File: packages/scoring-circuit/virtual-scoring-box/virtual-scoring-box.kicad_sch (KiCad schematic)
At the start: 0 parts

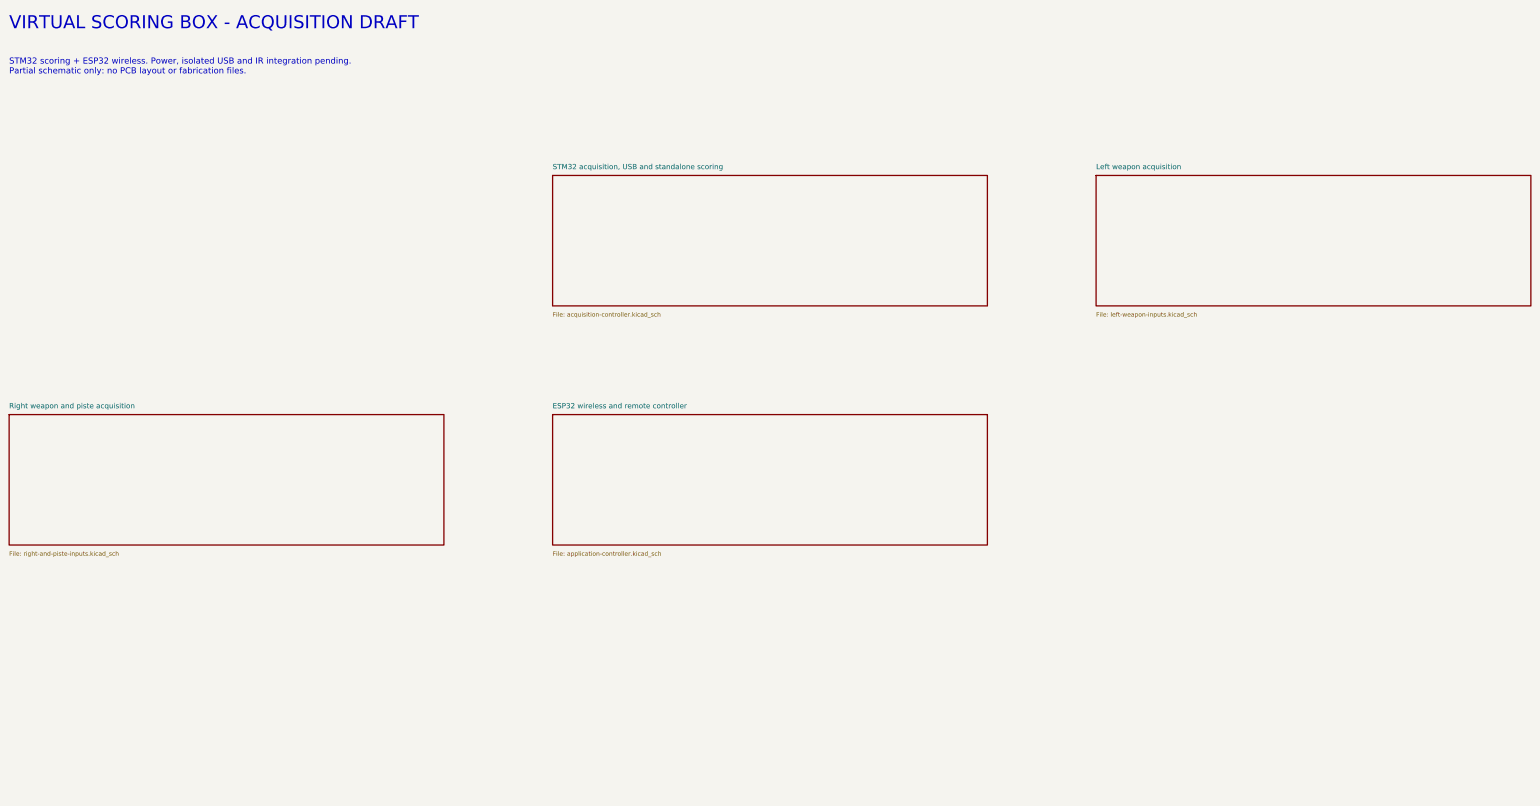
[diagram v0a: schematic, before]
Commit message: feat(scoring-circuit): place virtual scoring box input and controller circuits
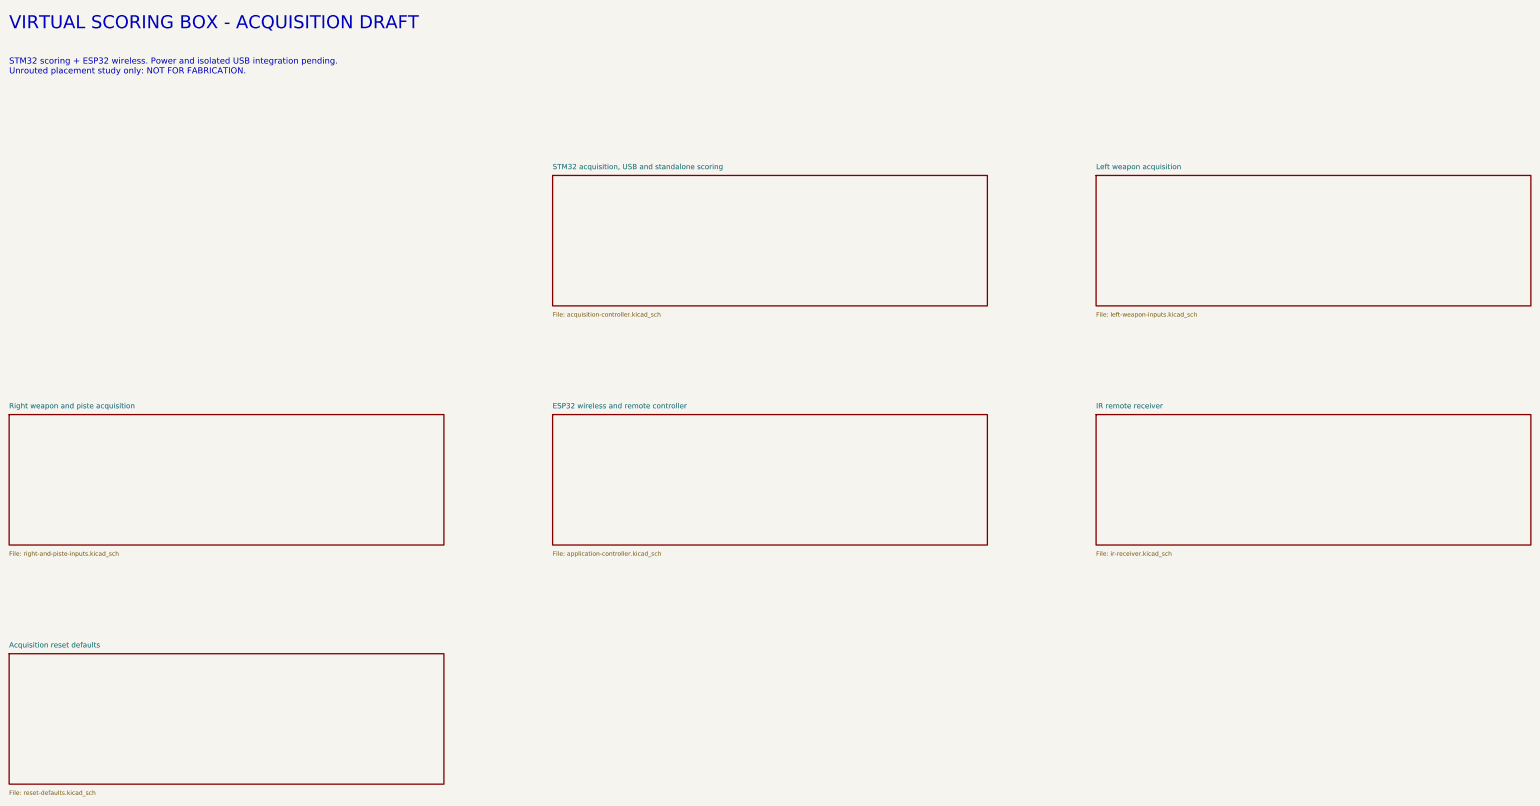
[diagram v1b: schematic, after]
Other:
- added sheet Acquisition reset defaults (reset-defaults.kicad_sch)
- added sheet IR remote receiver (ir-receiver.kicad_sch)
- note added: "STM32 scoring + ESP32 wireless. Power and isolated USB integration pending. Unrouted placement study only: NOT FOR FABRICATION."
- note removed: "STM32 scoring + ESP32 wireless. Power, isolated USB and IR integration pending. Partial schematic only: no PCB layout or fabrication files."
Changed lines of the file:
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@@
 (title_block (title "Virtual scoring box") (rev "Engineering draft") (comment 1 "Separate design - original prototype preserved"))
 (text "VIRTUAL SCORING BOX - ACQUISITION DRAFT" (at 30 20 0) (effects (font (size 3 3)) (justify left)))
-(text "STM32 scoring + ESP32 wireless. Power, isolated USB and IR integration pending.\nPartial schematic only: no PCB layout or fabrication files." (at 30 30 0) (effects (font (size 1.4 1.4)) (justify left)))
+(text "STM32 scoring + ESP32 wireless. Power and isolated USB integration pending.\nUnrouted placement study only: NOT FOR FABRICATION." (at 30 30 0) (effects (font (size 1.4 1.4)) (justify left)))
 (sheet (at 155 55) (size 100 30) (stroke (width 0.2) (type default)) (fill (color 0 0 0 0)) (property "Sheetname" "STM32 acquisition, USB and standalone scoring" (at 155 53 0) (effects (font (size 1.2 1.2)) (justify left))) (property "Sheetfile" "acquisition-controller.kicad_sch" (at 155 87 0) (effects (font (size 1 1)) (justify left))) (instances (project "virtual-scoring-box" (path "/20cc8167-128c-446a-a106-f942323e143f" (page "3")))))
 (sheet (at 280 55) (size 100 30) (stroke (width 0.2) (type default)) (fill (color 0 0 0 0)) (property "Sheetname" "Left weapon acquisition" (at 280 53 0) (effects (font (size 1.2 1.2)) (justify left))) (property "Sheetfile" "left-weapon-inputs.kicad_sch" (at 280 87 0) (effects (font (size 1 1)) (justify left))) (instances (project "virtual-scoring-box" (path "/20cc8167-128c-446a-a106-f942323e143f" (page "4")))))
@@
 (sheet_instances (path "/" (page "1")))
 (embedded_fonts no)
+(sheet (at 30 165) (size 100 30) (stroke (width 0.2) (type default)) (fill (color 0 0 0 0)) (property "Sheetname" "Acquisition reset defaults" (at 30 163 0) (effects (font (size 1.2 1.2)) (justify left))) (property "Sheetfile" "reset-defaults.kicad_sch" (at 30 197 0) (effects (font (size 1 1)) (justify left))) (instances (project "virtual-scoring-box" (path "/20cc8167-128c-446a-a106-f942323e143f" (page "8")))))
+(sheet (at 280 110) (size 100 30) (stroke (width 0.2) (type default)) (fill (color 0 0 0 0)) (property "Sheetname" "IR remote receiver" (at 280 108 0) (effects (font (size 1.2 1.2)) (justify left))) (property "Sheetfile" "ir-receiver.kicad_sch" (at 280 142 0) (effects (font (size 1 1)) (justify left))) (instances (project "virtual-scoring-box" (path "/20cc8167-128c-446a-a106-f942323e143f" (page "7")))))
 )

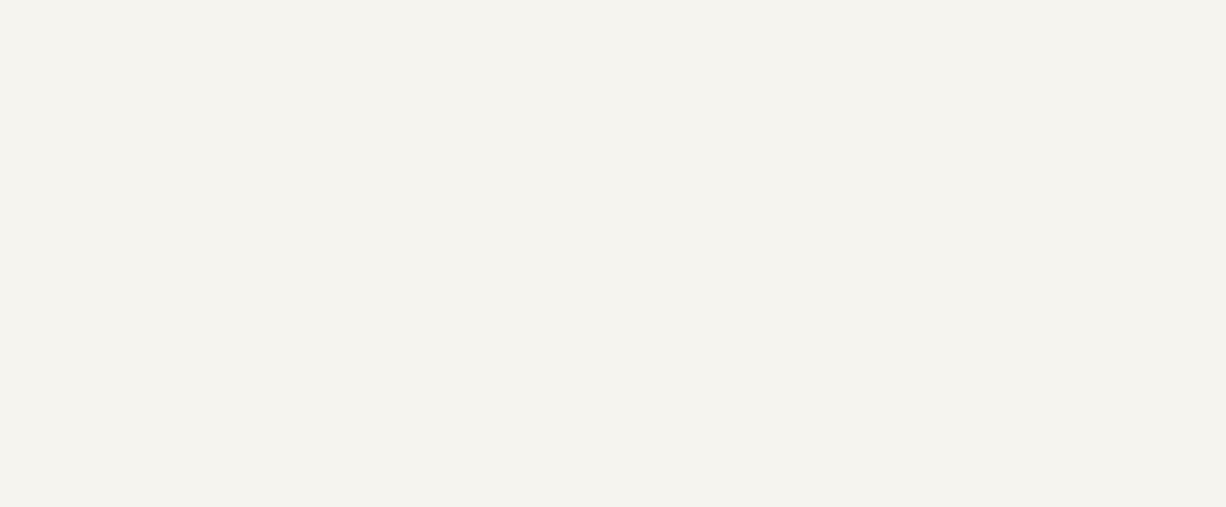
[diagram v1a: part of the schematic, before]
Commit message: feat(scoring-circuit): add virtual box USB interface and signal routing checkpoint
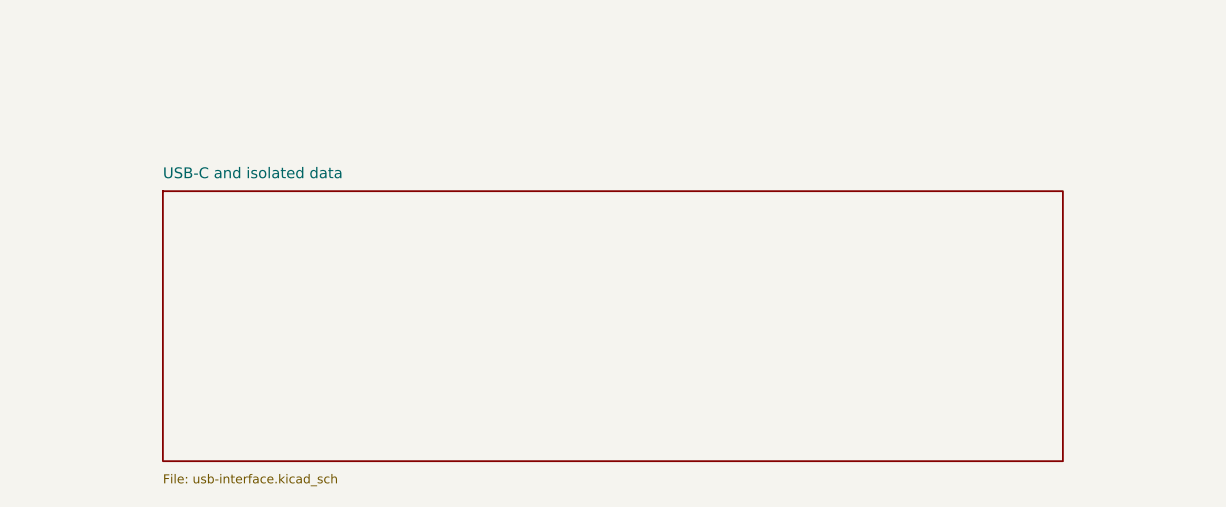
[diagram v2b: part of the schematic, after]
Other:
- added sheet USB-C and isolated data (usb-interface.kicad_sch)
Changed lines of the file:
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@@
 (sheet (at 30 110) (size 100 30) (stroke (width 0.2) (type default)) (fill (color 0 0 0 0)) (property "Sheetname" "Right weapon and piste acquisition" (at 30 108 0) (effects (font (size 1.2 1.2)) (justify left))) (property "Sheetfile" "right-and-piste-inputs.kicad_sch" (at 30 142 0) (effects (font (size 1 1)) (justify left))) (instances (project "virtual-scoring-box" (path "/20cc8167-128c-446a-a106-f942323e143f" (page "5")))))
 (sheet (at 155 110) (size 100 30) (stroke (width 0.2) (type default)) (fill (color 0 0 0 0)) (property "Sheetname" "ESP32 wireless and remote controller" (at 155 108 0) (effects (font (size 1.2 1.2)) (justify left))) (property "Sheetfile" "application-controller.kicad_sch" (at 155 142 0) (effects (font (size 1 1)) (justify left))) (instances (project "virtual-scoring-box" (path "/20cc8167-128c-446a-a106-f942323e143f" (page "6")))))
+(sheet (at 155 165) (size 100 30) (stroke (width 0.2) (type default)) (fill (color 0 0 0 0)) (property "Sheetname" "USB-C and isolated data" (at 155 163 0) (effects (font (size 1.2 1.2)) (justify left))) (property "Sheetfile" "usb-interface.kicad_sch" (at 155 197 0) (effects (font (size 1 1)) (justify left))) (instances (project "virtual-scoring-box" (path "/20cc8167-128c-446a-a106-f942323e143f" (page "9")))))
 (sheet_instances (path "/" (page "1")))
 (embedded_fonts no)

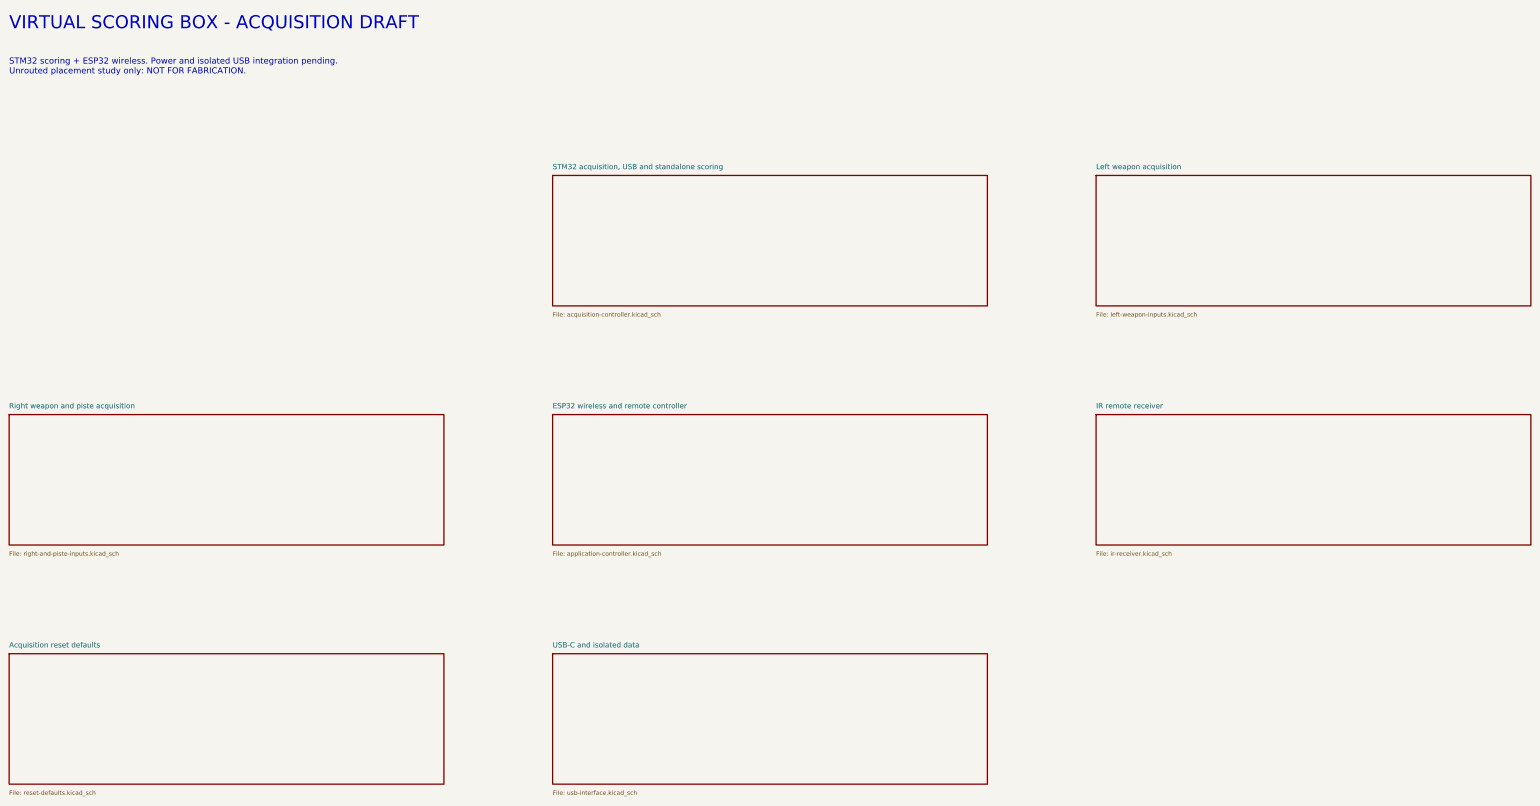
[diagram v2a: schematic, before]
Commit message: feat(scoring-circuit): integrate isolated virtual-box processor supply
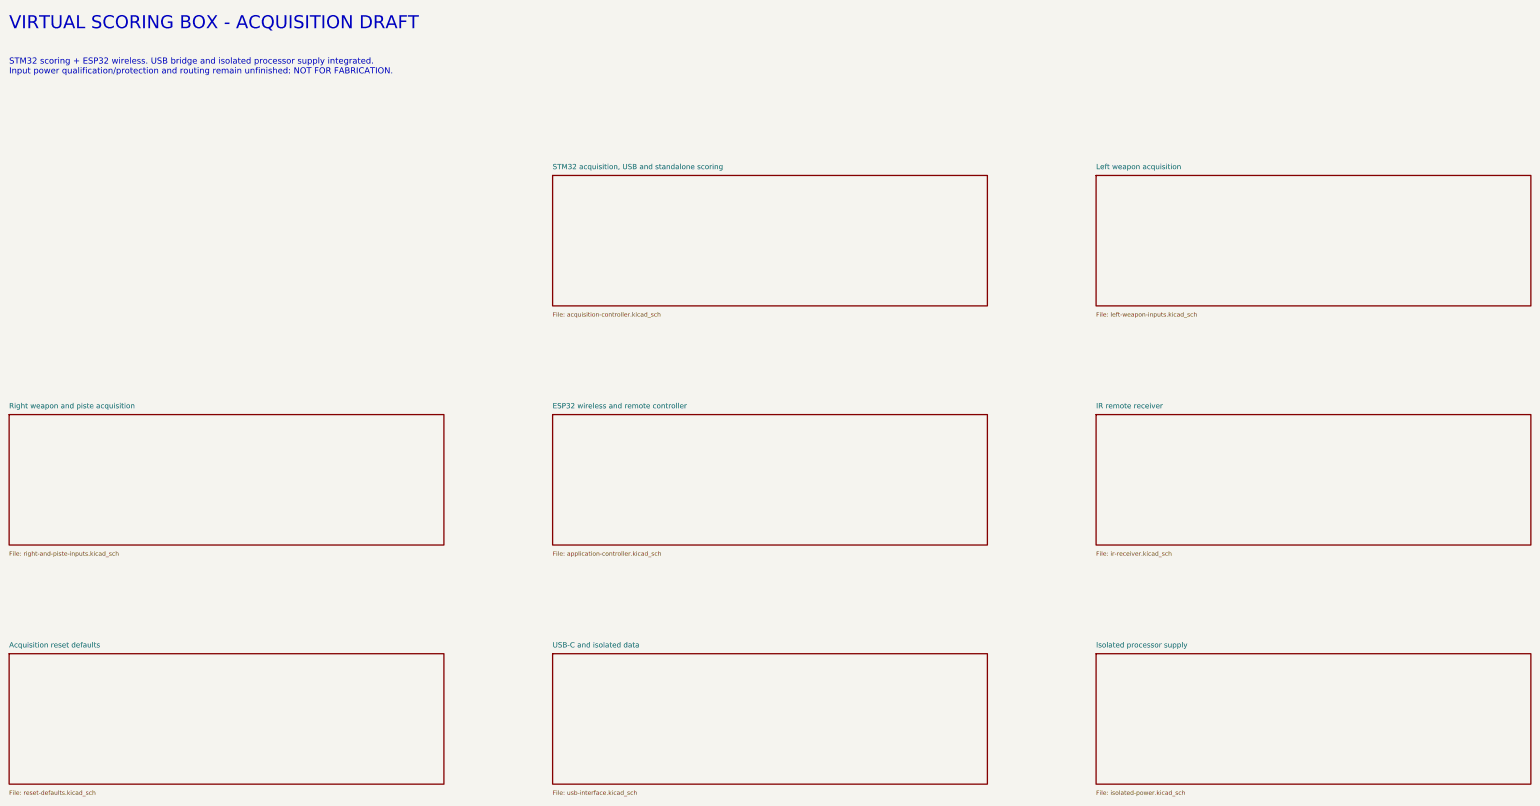
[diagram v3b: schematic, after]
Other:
- added sheet Isolated processor supply (isolated-power.kicad_sch)
- note added: "STM32 scoring + ESP32 wireless. USB bridge and isolated processor supply integrated. Input power qualification/protection and routing remain unfinished: NOT FOR FABRICATION."
- note removed: "STM32 scoring + ESP32 wireless. Power and isolated USB integration pending. Unrouted placement study only: NOT FOR FABRICATION."
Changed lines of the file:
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@@
-(kicad_sch (version 20250114)
+(kicad_sch
+(version 20250114)
 (generator "eeschema")
 (paper "A3")
 (title_block (title "Virtual scoring box") (rev "Engineering draft") (comment 1 "Separate design - original prototype preserved"))
 (text "VIRTUAL SCORING BOX - ACQUISITION DRAFT" (at 30 20 0) (effects (font (size 3 3)) (justify left)))
-(text "STM32 scoring + ESP32 wireless. Power and isolated USB integration pending.\nUnrouted placement study only: NOT FOR FABRICATION." (at 30 30 0) (effects (font (size 1.4 1.4)) (justify left)))
+(text "STM32 scoring + ESP32 wireless. USB bridge and isolated processor supply integrated.\nInput power qualification/protection and routing remain unfinished: NOT FOR FABRICATION." (at 30 30 0) (effects (font (size 1.4 1.4)) (justify left)))
 (sheet (at 155 55) (size 100 30) (stroke (width 0.2) (type default)) (fill (color 0 0 0 0)) (property "Sheetname" "STM32 acquisition, USB and standalone scoring" (at 155 53 0) (effects (font (size 1.2 1.2)) (justify left))) (property "Sheetfile" "acquisition-controller.kicad_sch" (at 155 87 0) (effects (font (size 1 1)) (justify left))) (instances (project "virtual-scoring-box" (path "/20cc8167-128c-446a-a106-f942323e143f" (page "3")))))
 (sheet (at 280 55) (size 100 30) (stroke (width 0.2) (type default)) (fill (color 0 0 0 0)) (property "Sheetname" "Left weapon acquisition" (at 280 53 0) (effects (font (size 1.2 1.2)) (justify left))) (property "Sheetfile" "left-weapon-inputs.kicad_sch" (at 280 87 0) (effects (font (size 1 1)) (justify left))) (instances (project "virtual-scoring-box" (path "/20cc8167-128c-446a-a106-f942323e143f" (page "4")))))
@@
 (sheet (at 30 165) (size 100 30) (stroke (width 0.2) (type default)) (fill (color 0 0 0 0)) (property "Sheetname" "Acquisition reset defaults" (at 30 163 0) (effects (font (size 1.2 1.2)) (justify left))) (property "Sheetfile" "reset-defaults.kicad_sch" (at 30 197 0) (effects (font (size 1 1)) (justify left))) (instances (project "virtual-scoring-box" (path "/20cc8167-128c-446a-a106-f942323e143f" (page "8")))))
 (sheet (at 280 110) (size 100 30) (stroke (width 0.2) (type default)) (fill (color 0 0 0 0)) (property "Sheetname" "IR remote receiver" (at 280 108 0) (effects (font (size 1.2 1.2)) (justify left))) (property "Sheetfile" "ir-receiver.kicad_sch" (at 280 142 0) (effects (font (size 1 1)) (justify left))) (instances (project "virtual-scoring-box" (path "/20cc8167-128c-446a-a106-f942323e143f" (page "7")))))
+(sheet (at 280 165) (size 100 30) (stroke (width .2) (type default)) (fill (color 0 0 0 0)) (property "Sheetname" "Isolated processor supply" (at 280 163 0) (effects (font (size 1.2 1.2)) (justify left))) (property "Sheetfile" "isolated-power.kicad_sch" (at 280 197 0) (effects (font (size 1 1)) (justify left))) (instances (project "virtual-scoring-box" (path "/20cc8167-128c-446a-a106-f942323e143f" (page "10")))))
 )
